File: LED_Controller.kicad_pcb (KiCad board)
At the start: 2 copper layers, 127 x 101.6 mm, 25 parts, among them CON1 CONNECTOR, CON2 CONNECTOR, CON3 CONNECTOR, CON4 CONNECTOR, CON5 PWR_CON, CON6 AVR-ISP-10, CON7 AVR-ISP-6, IC1 ATMEGA328P-P, Q1 STS8DN3LLH5, Q2 STS8DN3LLH5, Q3 STS8DN3LLH5

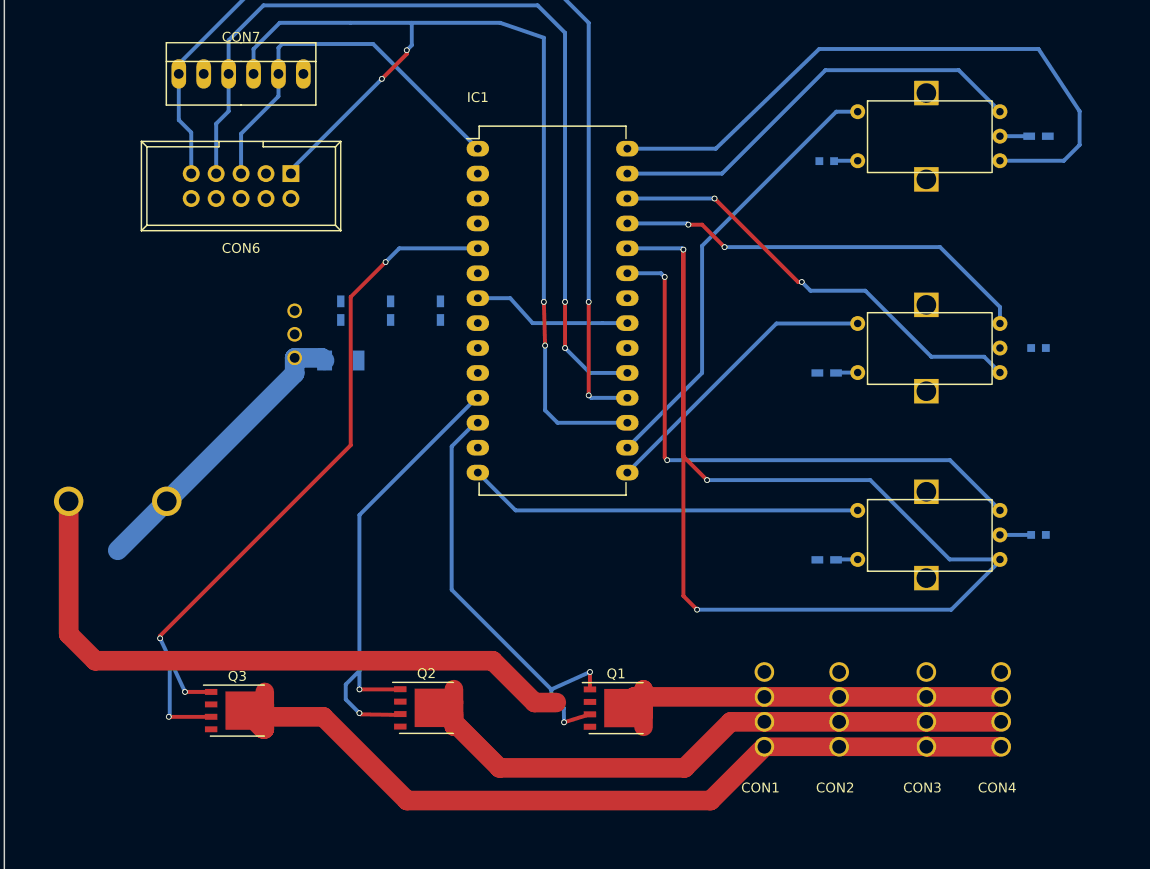
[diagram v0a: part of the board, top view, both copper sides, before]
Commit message: Minor Changes
Added a pull-up resistor to RST, to ensure chip is not reset during
normal use. Some minor changes to the track layout.
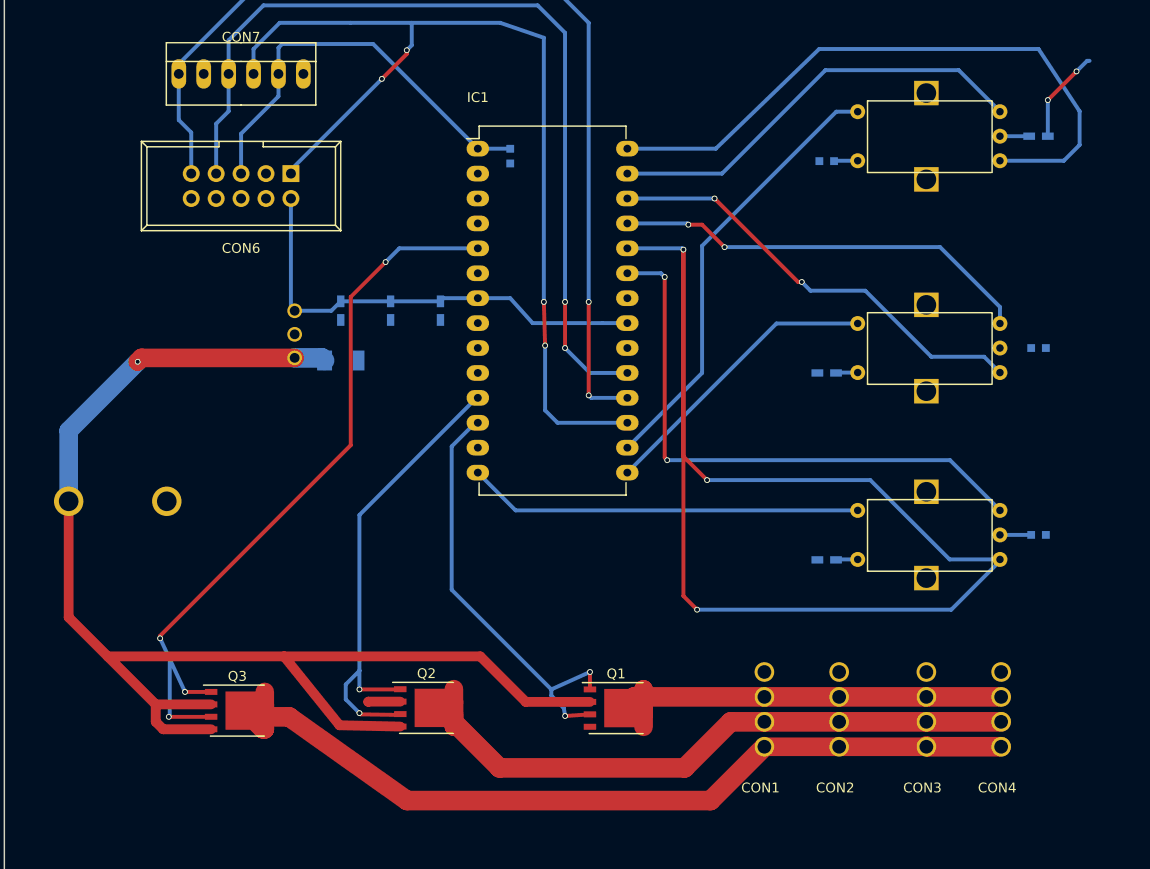
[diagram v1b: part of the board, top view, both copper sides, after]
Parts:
- added R7: 10k, LEDs:LED_0603, B.Cu at (129.0, 78.2)
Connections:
- CON5 pad 1: +12V -> Net-(CON5-Pad1)
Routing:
- net +5V: track 16.4 -> 47.2 mm
- net +12V: track 96.4 -> 124.8 mm, vias 0 -> 1
- net Net-(CON5-Pad1): track 0.00 -> 19.0 mm
- net GND: track 0.00 -> 9.60 mm, vias 0 -> 2
- net /RST: track 39.3 -> 42.6 mm
- net /BLUE_5V: track 45.4 -> 44.5 mm
- net /RED_12V: track 90.1 -> 89.3 mm
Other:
- net class 1mm added: clearance 0.45, trace_width 1, via_dia 0.6, via_drill 0.4

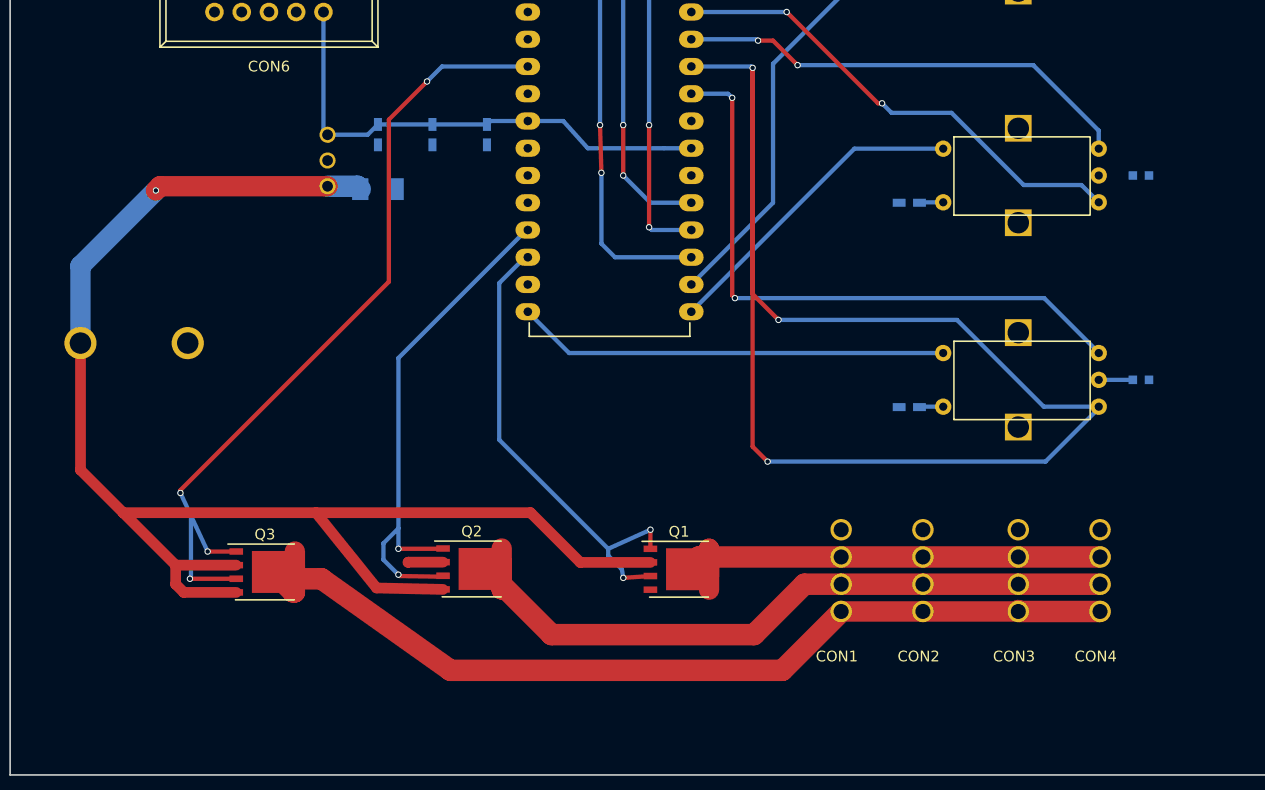
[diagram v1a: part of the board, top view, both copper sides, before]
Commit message: Changed to Common Anode, new status LEDs
Updated schematic to reflect common anode LED strip, instead of common
cathode.

Added indicator LEDs to 12V and 5V power supply.

Other minor routing changes. Still need to update footprint to make
rotary encoder pins larger and probably change the Atmega footprint to
the correct size.
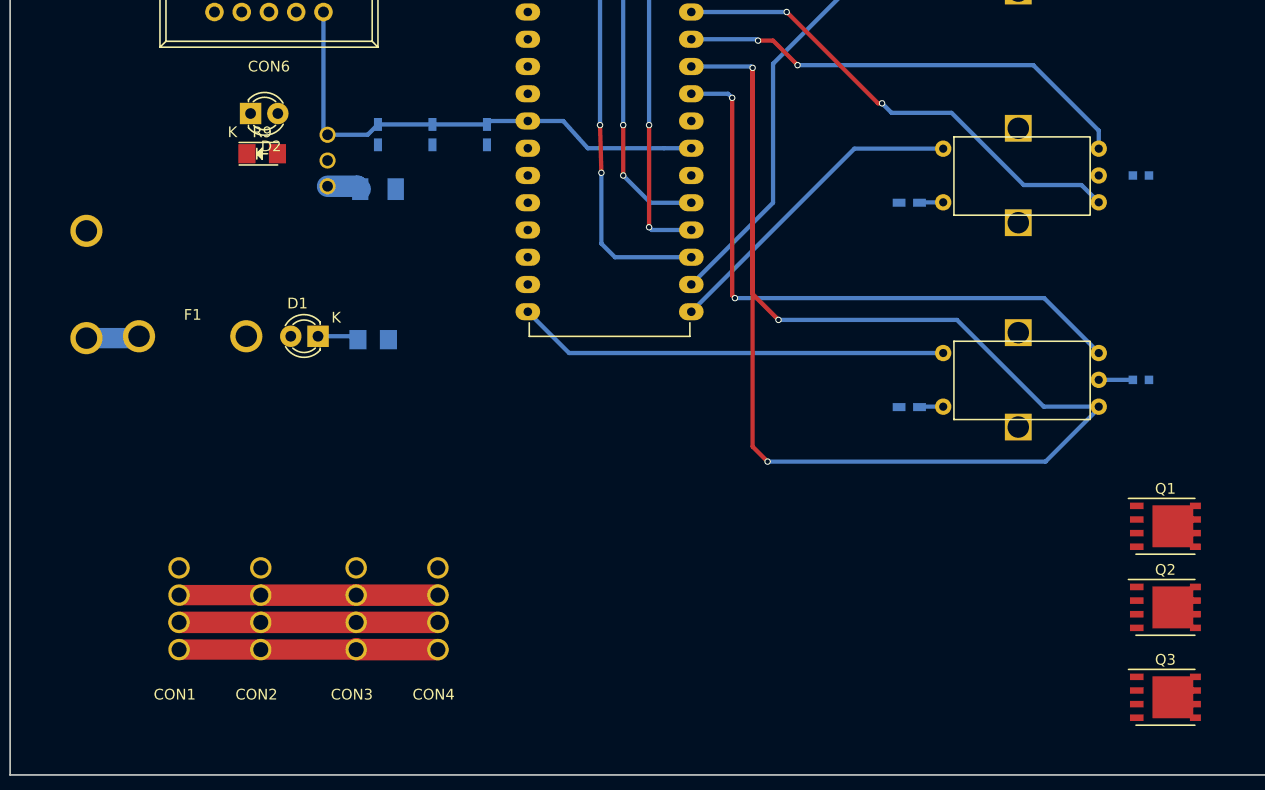
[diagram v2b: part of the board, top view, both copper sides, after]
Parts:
- added D1: LED, LEDs:LED-3MM, F.Cu at (106.2, 112.8)
- added D2: LED, LEDs:LED-3MM, F.Cu at (99.9, 92.0)
- added F1: FUSE, LED_controller_footprints:12V_PWR_HOLES, F.Cu at (94.5, 112.8)
- added R8: 820, LEDs:LED_1206, B.Cu at (111.3, 113.1)
- added R9: 499, LEDs:LED_1206, F.Cu at (101.0, 95.8)
- moved Q3 84.8 mm to (185.2, 146.4)
- moved Q2 64.8 mm to (185.2, 138.0)
- moved CON2 61.8 mm to (100.8, 138.2)
- moved CON1 61.8 mm to (93.2, 138.2)
- moved CON3 61.8 mm to (109.7, 138.2)
- moved CON4 61.8 mm to (117.3, 138.2)
- moved Q1 45.5 mm to (185.2, 130.5)
- moved CON5 7.04 mm to (84.6, 108.0), turned to 90 degrees
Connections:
- CON1 pad 1: /RED_12V -> /RED_PWR
- CON1 pad 2: /GREEN_12V -> /GREEN_PWR
- CON1 pad 3: /BLUE_12V -> /BLUE_PWR
- CON1 pad 4: GND -> +12V
- CON2 pad 1: /RED_12V -> /RED_PWR
- CON2 pad 2: /GREEN_12V -> /GREEN_PWR
- CON2 pad 3: /BLUE_12V -> /BLUE_PWR
- CON2 pad 4: GND -> +12V
- CON3 pad 1: /RED_12V -> /RED_PWR
- CON3 pad 2: /GREEN_12V -> /GREEN_PWR
- CON3 pad 3: /BLUE_12V -> /BLUE_PWR
- CON3 pad 4: GND -> +12V
- CON4 pad 1: /RED_12V -> /RED_PWR
- CON4 pad 2: /GREEN_12V -> /GREEN_PWR
- CON4 pad 3: /BLUE_12V -> /BLUE_PWR
- CON5 pad 1: Net-(CON5-Pad1) -> +12V
- Q1 pad 1: /BLUE_5V -> /BLUE_PWR
- Q1 pad 2: +12V -> /BLUE_12V
- Q1 pad 3: /BLUE_5V -> /BLUE_PWR
- Q1 pad 4: +12V -> /BLUE_12V
- Q1 pad 5: /BLUE_12V -> GND
- Q2 pad 2: +12V -> /GREEN_PWR
- Q2 pad 4: +12V -> /GREEN_PWR
- Q2 pad 5: /GREEN_12V -> GND
- Q3 pad 2: +12V -> /RED_PWR
- Q3 pad 4: +12V -> /RED_PWR
- Q3 pad 5: /RED_12V -> GND
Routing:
- net +12V: track 124.8 -> 8.14 mm, vias 1 -> 0
- net /RED_12V: track 89.3 -> 0.00 mm
- net /RED_5V: track 76.8 -> 0.00 mm, vias 4 -> 0
- net /GREEN_12V: track 71.7 -> 0.00 mm
- net /GREEN_5V: track 49.2 -> 0.64 mm, vias 2 -> 0
- net /BLUE_12V: track 47.7 -> 0.00 mm
- net /BLUE_5V: track 44.5 -> 0.25 mm, vias 2 -> 0
- net /RED_PWR: track 0.00 -> 24.2 mm
- net /GREEN_PWR: track 0.00 -> 24.1 mm
- net /BLUE_PWR: track 0.00 -> 24.1 mm
- net Net-(CON5-Pad1): track 19.0 -> 0.00 mm
- net Net-(D1-Pad1): track 0.00 -> 3.77 mm

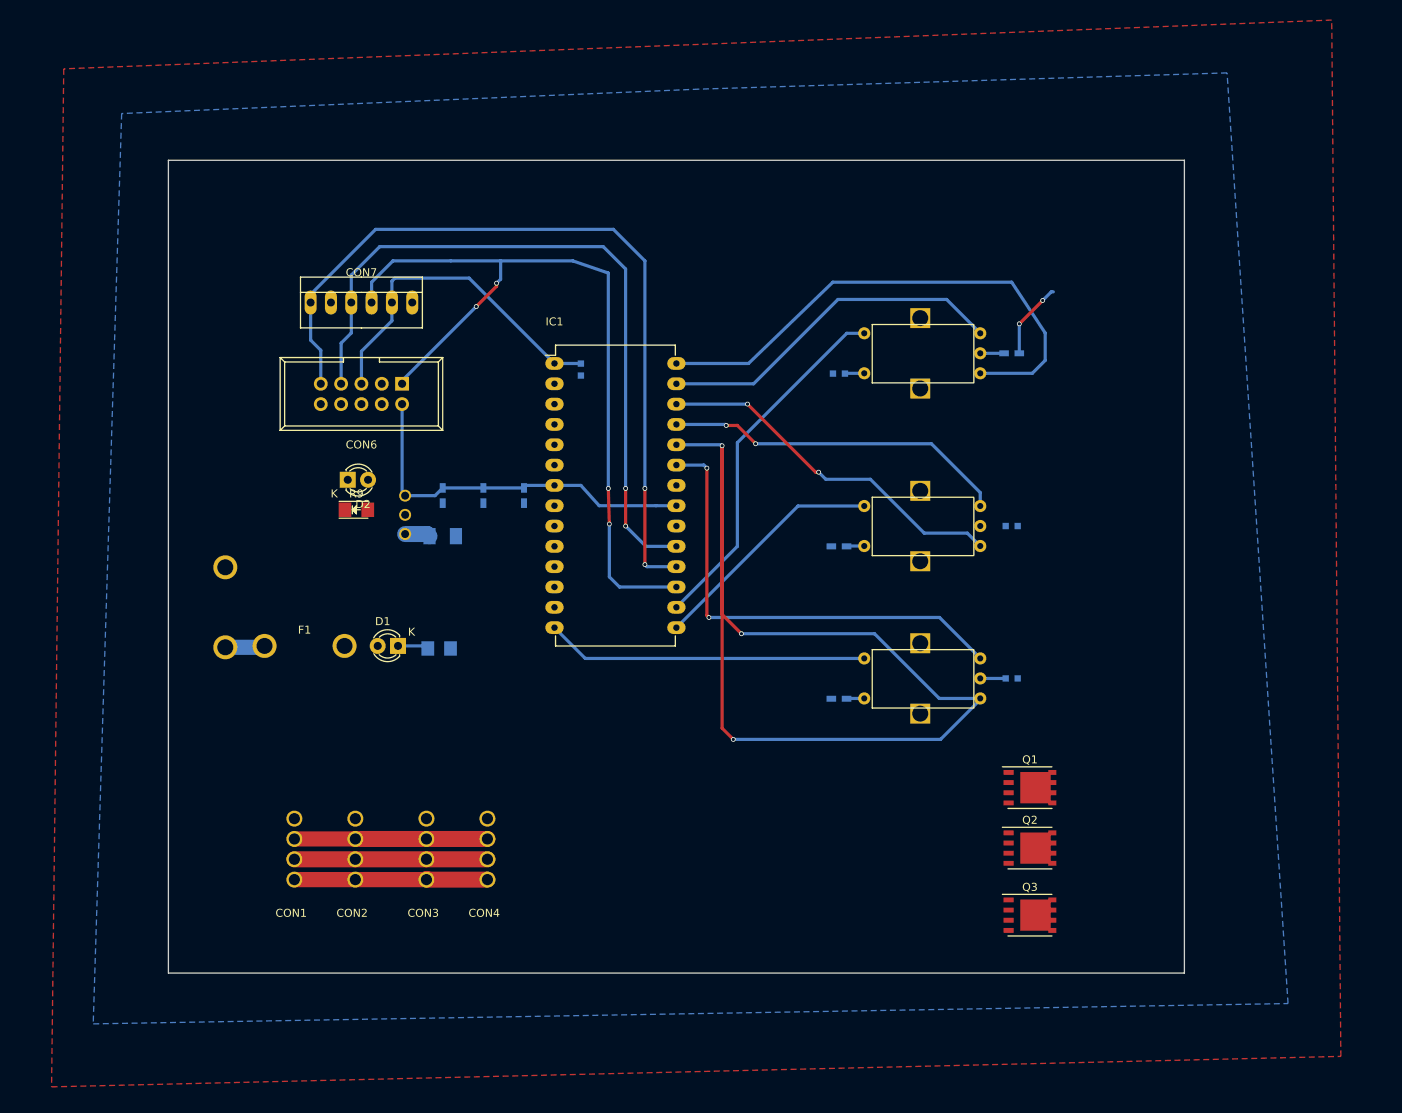
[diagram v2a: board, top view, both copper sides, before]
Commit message: Atmega footprint updated, SS Pin changed, Heatsink footprint added
Atmega328p footprint now correct size

Added SS pin for SPI

Made and placed footprint for 50mm square heatsink
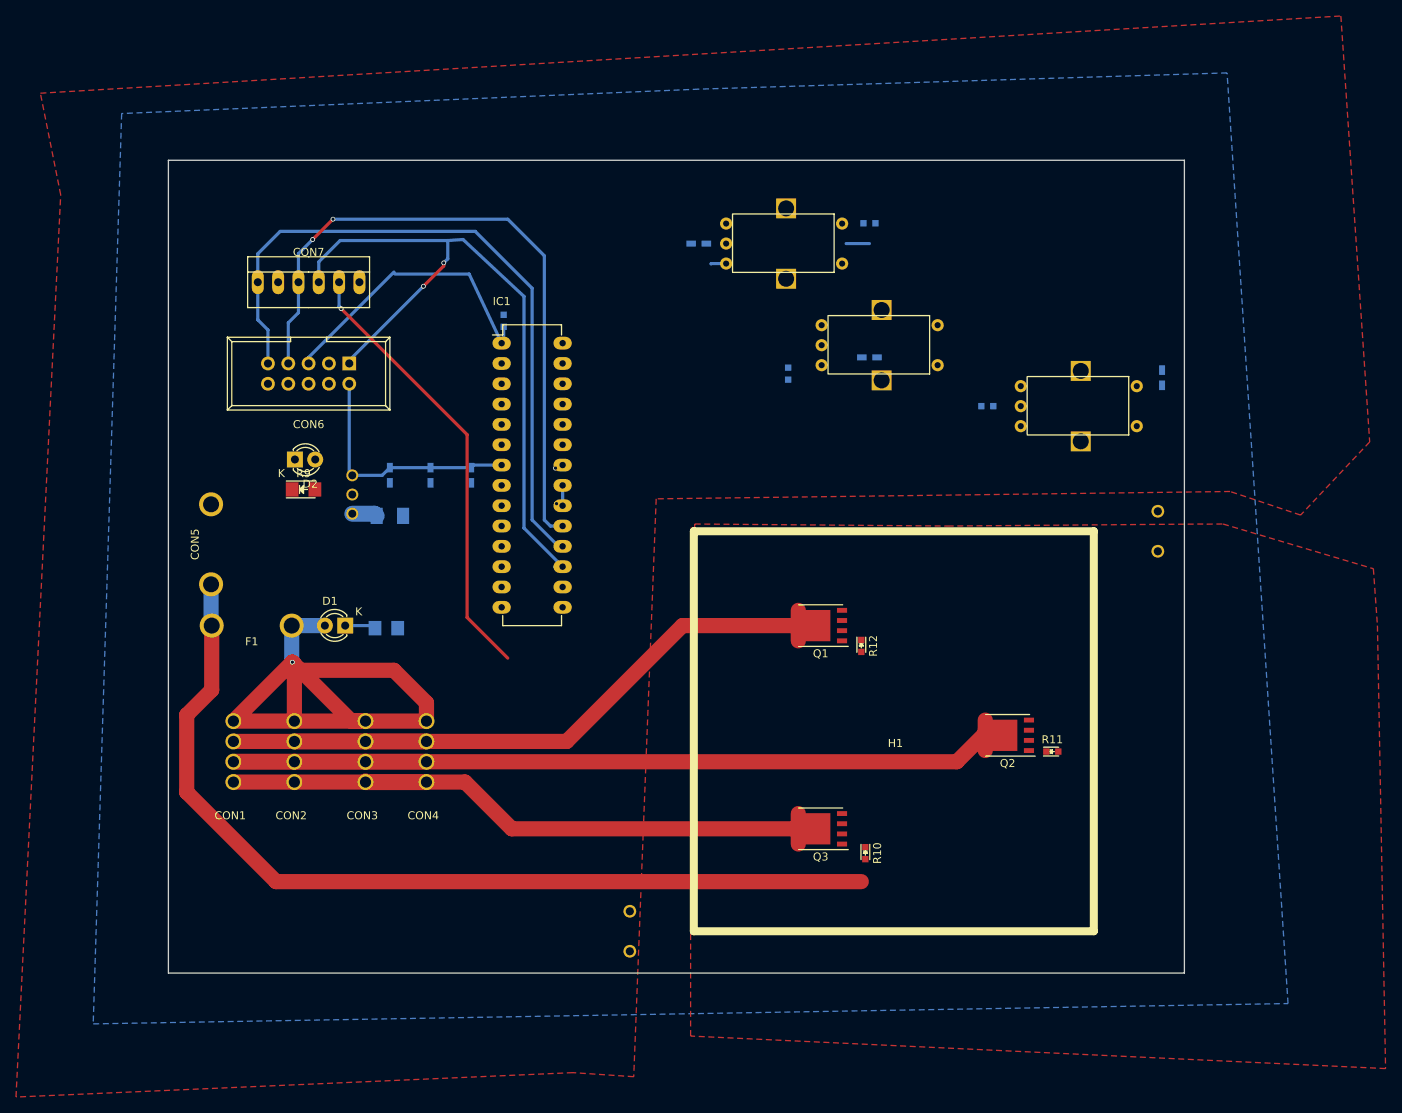
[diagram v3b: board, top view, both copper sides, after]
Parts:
- added H1: Heatsink_50x50mm, LED_controller_footprints:Heatsink_50x50mm, F.Cu at (168.1, 123.4)
- added R10: 10k, LEDs:LED_0603, F.Cu at (164.6, 138.7)
- added R11: 10k, LEDs:LED_0603, F.Cu at (188.0, 126.0)
- added R12: 10k, LEDs:LED_0603, F.Cu at (164.1, 112.8)
- CON5: moved to F.Cu
- IC1: footprint Housings_DIP:DIP-28_W15.24mm_LongPads -> Housings_DIP:DIP-28_W7.62mm_LongPads
- moved R4 56.9 mm to (201.7, 79.2), turned to 270 degrees
- moved R3 41.5 mm to (143.8, 62.5), turned to 180 degrees
- moved E1 39.5 mm to (191.5, 82.8), turned to 180 degrees
- moved R1 34.2 mm to (179.8, 82.8), turned to 180 degrees
- moved R2 33.8 mm to (154.9, 78.7), turned to 270 degrees
- moved Q1 33.1 mm to (159.0, 110.2), turned to 180 degrees
- moved Q3 28.3 mm to (159.0, 135.6), turned to 180 degrees
- moved R5 23.9 mm to (165.1, 76.7), turned to 180 degrees
- moved E2 23.1 mm to (166.6, 75.2), turned to 180 degrees
- moved E3 21.7 mm to (154.7, 62.5), turned to 180 degrees
- moved R6 19.2 mm to (165.1, 59.9), turned to 180 degrees
- moved CON1 14.4 mm to (85.6, 126.0)
- moved CON4 14.4 mm to (109.7, 126.0)
- moved CON2 14.4 mm to (93.2, 126.0)
- moved CON3 14.4 mm to (102.1, 126.0)
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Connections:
- CON4 pad 4: GND -> +12V
- CON5 pad 1: +12V -> Net-(CON5-Pad1)
- CON7 pad 5: /RST -> /SS
- IC1 pad 10: Net-(IC1-Pad10) -> Net-(E3-Pad1)
- IC1 pad 16: Net-(E3-Pad1) -> /SS
- Q1 pad 1: /BLUE_PWR -> /BLUE_5V
- Q1 pad 2: /BLUE_12V -> GND
- Q1 pad 3: /BLUE_PWR -> /BLUE_5V
- Q1 pad 4: /BLUE_12V -> GND
- Q1 pad 5: GND -> /BLUE_PWR
- Q2 pad 2: /GREEN_PWR -> GND
- Q2 pad 4: /GREEN_PWR -> GND
- Q2 pad 5: GND -> /GREEN_PWR
- Q3 pad 2: /RED_PWR -> GND
- Q3 pad 4: /RED_PWR -> GND
- Q3 pad 5: GND -> /RED_PWR
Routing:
- net Net-(E1-Pad5): track 133.8 -> 0.00 mm, vias 3 -> 0
- net Net-(CON5-Pad1): track 0.00 -> 116.4 mm
- net +12V: track 8.14 -> 85.8 mm, vias 0 -> 1
- net /GREEN_PWR: track 24.1 -> 99.9 mm
- net Net-(E3-Pad5): track 65.8 -> 0.00 mm
- net Net-(E1-Pad4): track 58.8 -> 0.00 mm, vias 2 -> 0
- net /BLUE_PWR: track 24.1 -> 80.2 mm
- net /SS: track 0.00 -> 55.7 mm, vias 0 -> 1
- net /RED_PWR: track 24.2 -> 76.6 mm
- net Net-(E2-Pad5): track 45.3 -> 0.00 mm, vias 2 -> 0
- net Net-(E3-Pad1): track 45.3 -> 0.00 mm
- net Net-(E2-Pad4): track 43.2 -> 0.00 mm, vias 2 -> 0
- net Net-(E3-Pad4): track 44.1 -> 2.41 mm
- net Net-(E1-Pad1): track 40.3 -> 0.00 mm
- net Net-(E2-Pad1): track 29.8 -> 0.00 mm
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- added copper zone on F.Cu, net +12V
